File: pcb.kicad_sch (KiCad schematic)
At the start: 194 parts

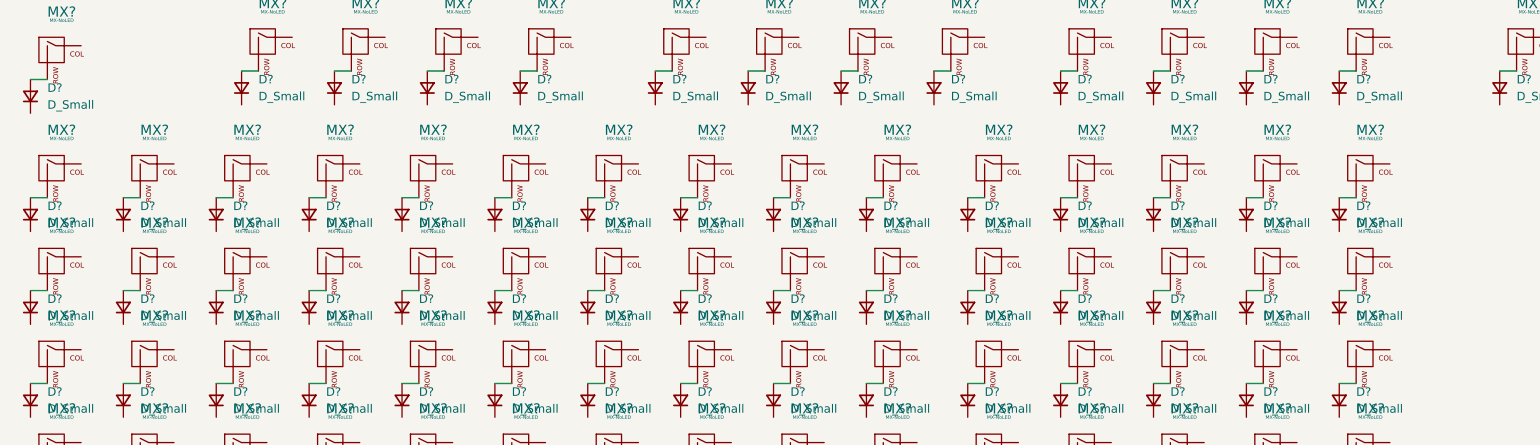
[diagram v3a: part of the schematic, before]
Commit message: edit switchgrid schem a bit
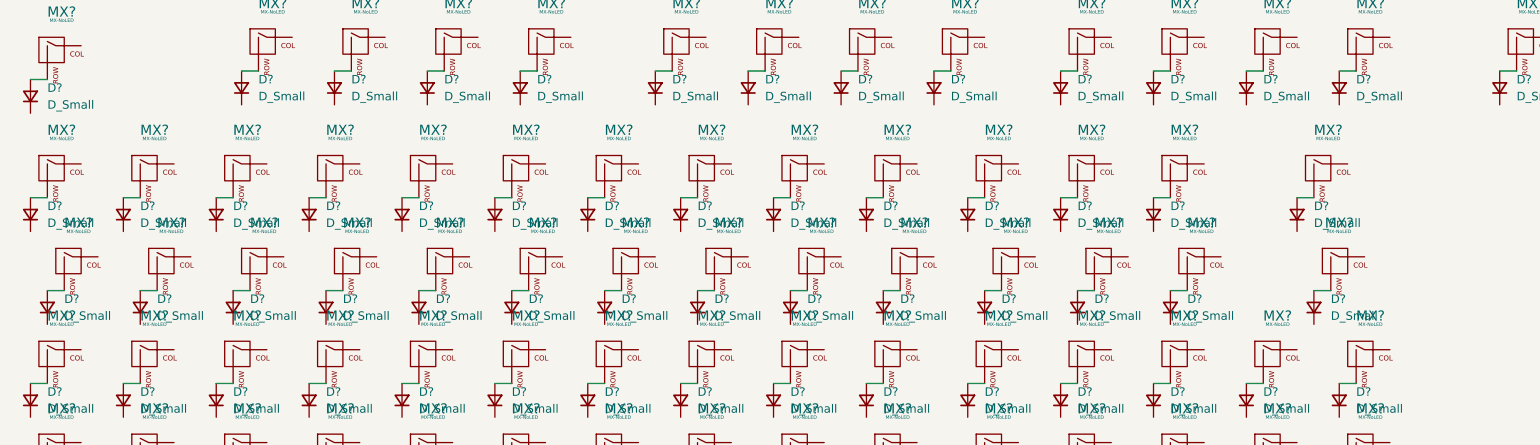
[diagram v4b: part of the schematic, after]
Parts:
- removed D? (x2): D_Small, symbol Device:D_Small
- removed MX? (x2): MX-NoLED, symbol MX_Alps_Hybrid:MX-NoLED
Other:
- moved on the sheet: D?, MX?
